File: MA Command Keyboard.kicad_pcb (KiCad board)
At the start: 2 copper layers, 195.3 x 209.6 mm, 165 parts, among them SW1 SW_Push, U1 ATmega32U4-A, Y1 16MHz

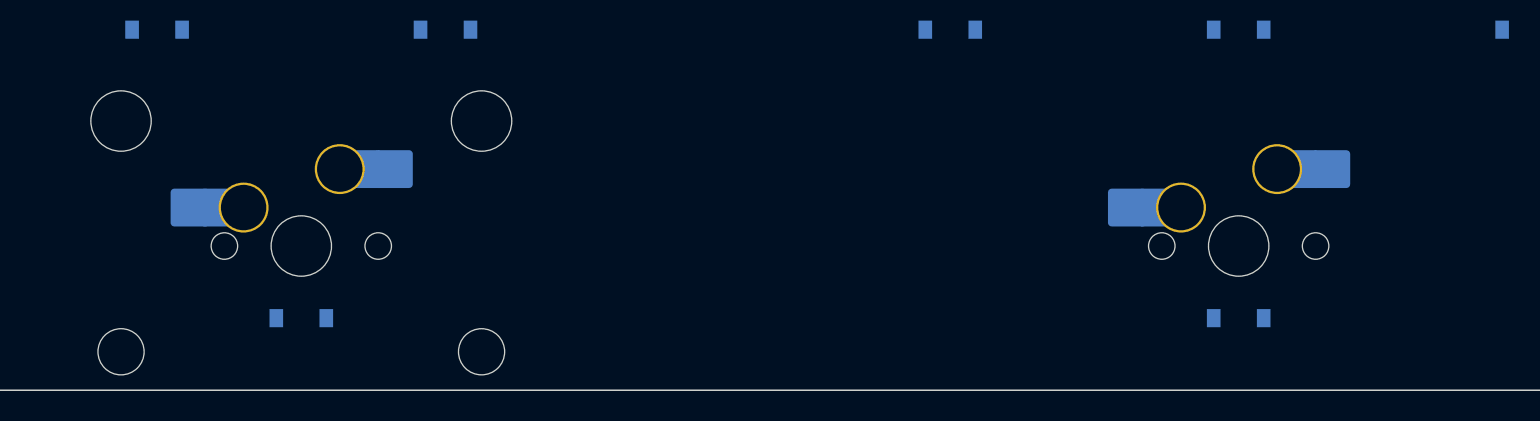
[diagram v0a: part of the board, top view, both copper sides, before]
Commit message: Updated Placement
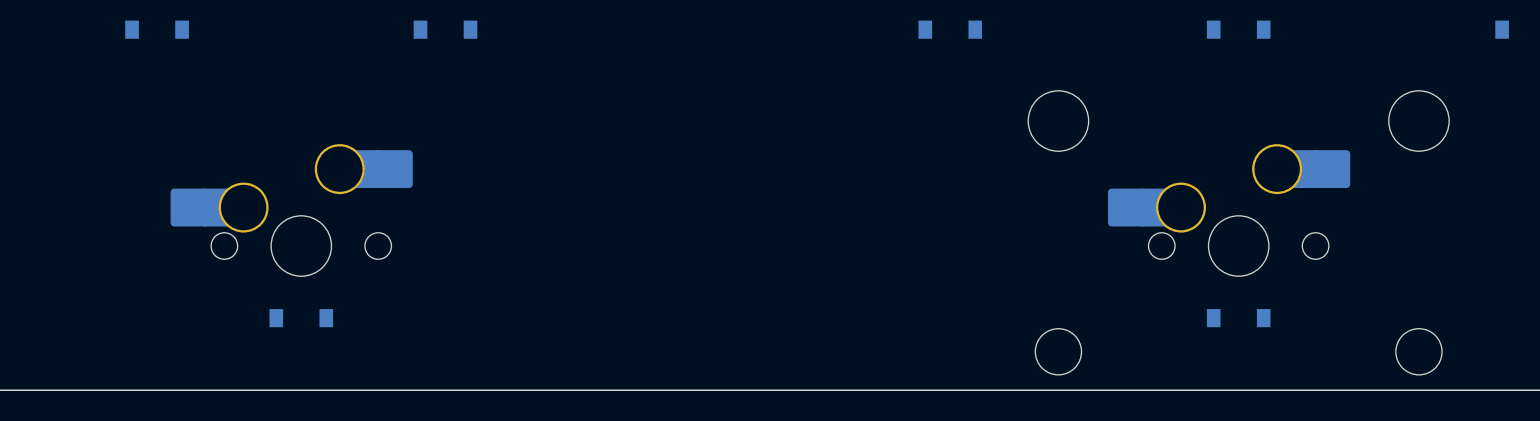
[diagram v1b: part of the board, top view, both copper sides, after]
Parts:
- moved D25 133.7 mm to (-327.0, 127.0)
- moved MX25 133.7 mm to (-327.0, 122.2)
- moved D63 114.7 mm to (-188.9, 231.8)
- moved MX63 114.7 mm to (-188.9, 227.0)
- moved D64 111.2 mm to (-169.9, 212.7)
- moved MX64 111.2 mm to (-169.9, 208.0)
- moved D65 109.5 mm to (-150.8, 231.8)
- moved MX65 109.5 mm to (-150.8, 227.0)
- moved D62 105.2 mm to (-222.2, 212.7)
- moved MX62 105.2 mm to (-222.2, 208.0)
- moved D71 95.2 mm to (-231.8, 250.8)
- moved MX71 95.2 mm to (-231.8, 246.1)
- moved D69 90.5 mm to (-260.4, 231.8)
- moved D70 90.5 mm to (-241.3, 231.8)
- moved MX69 90.5 mm to (-260.4, 227.0)
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
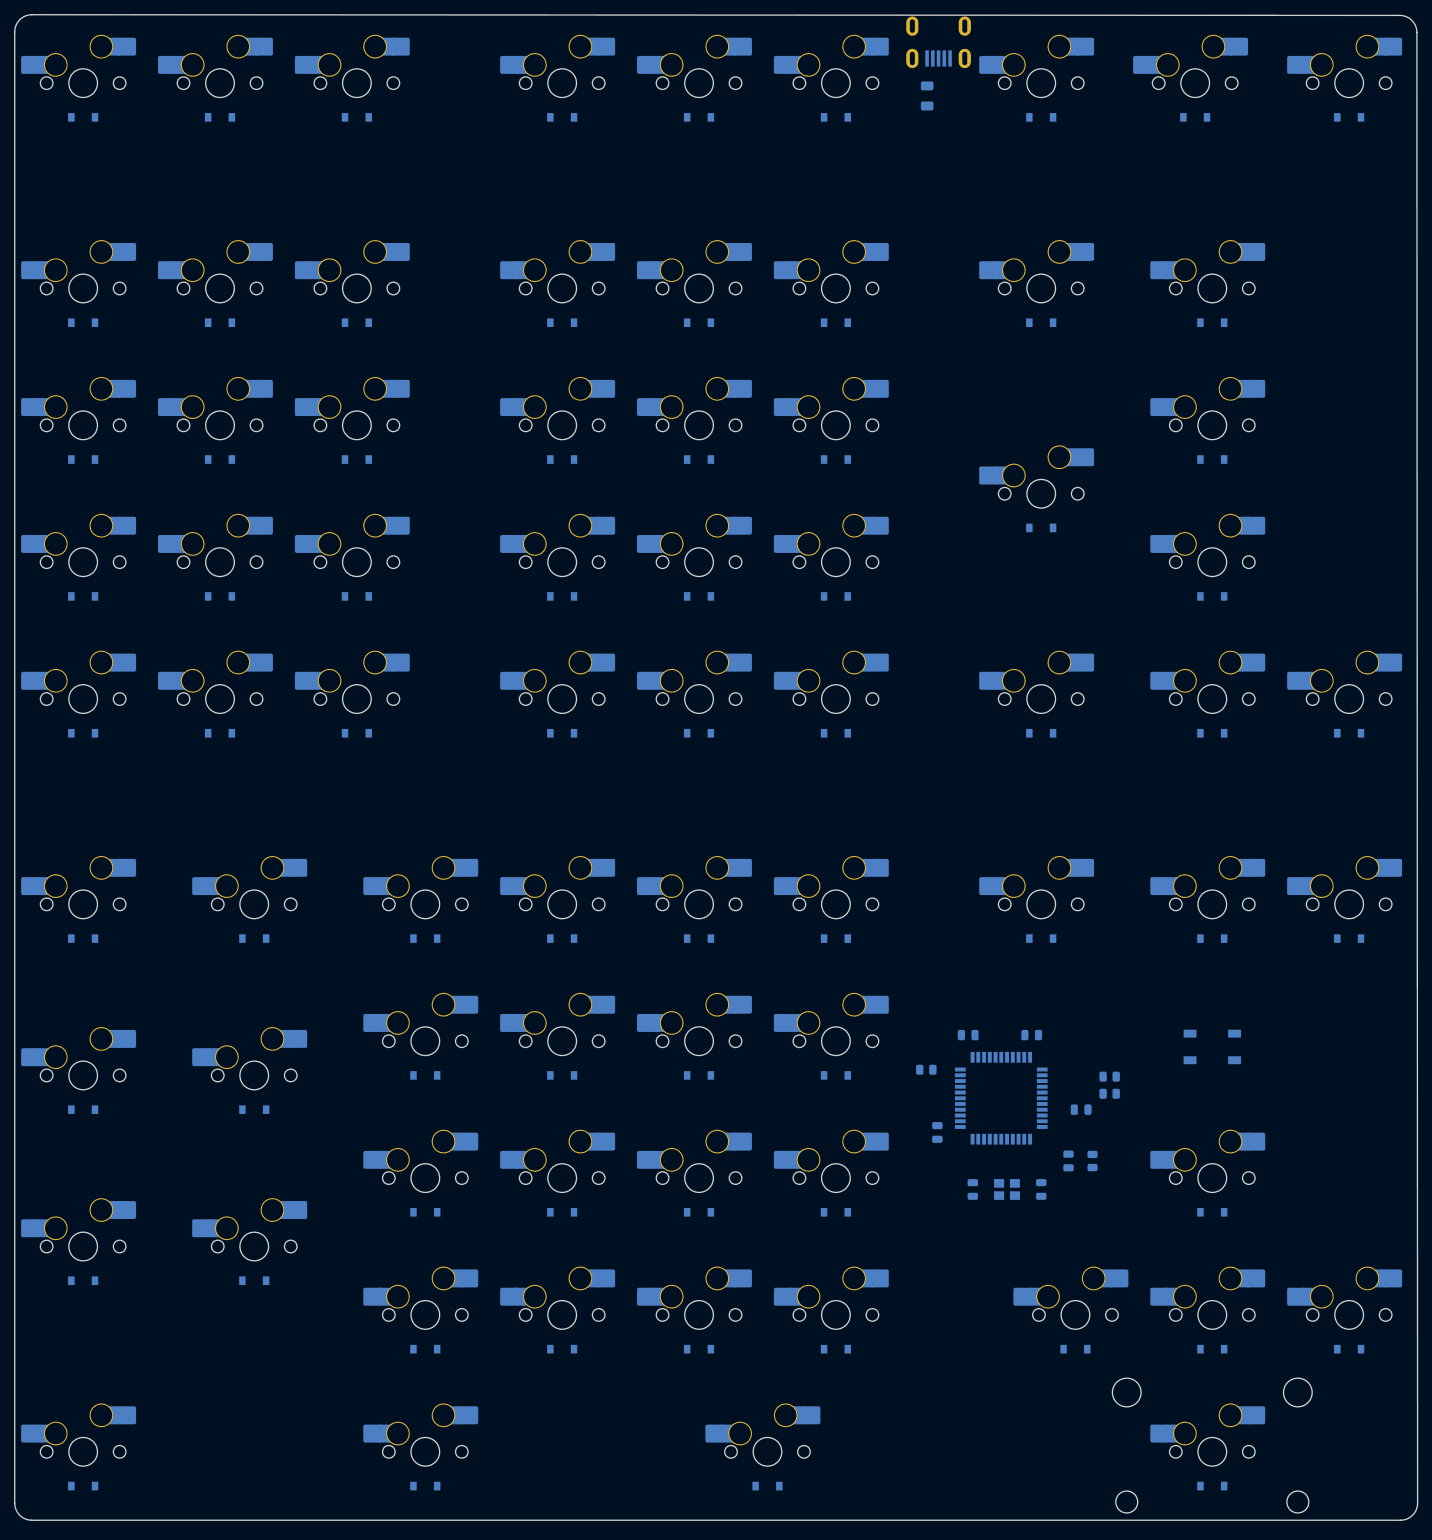
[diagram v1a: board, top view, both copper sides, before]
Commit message: Matrix Traces in
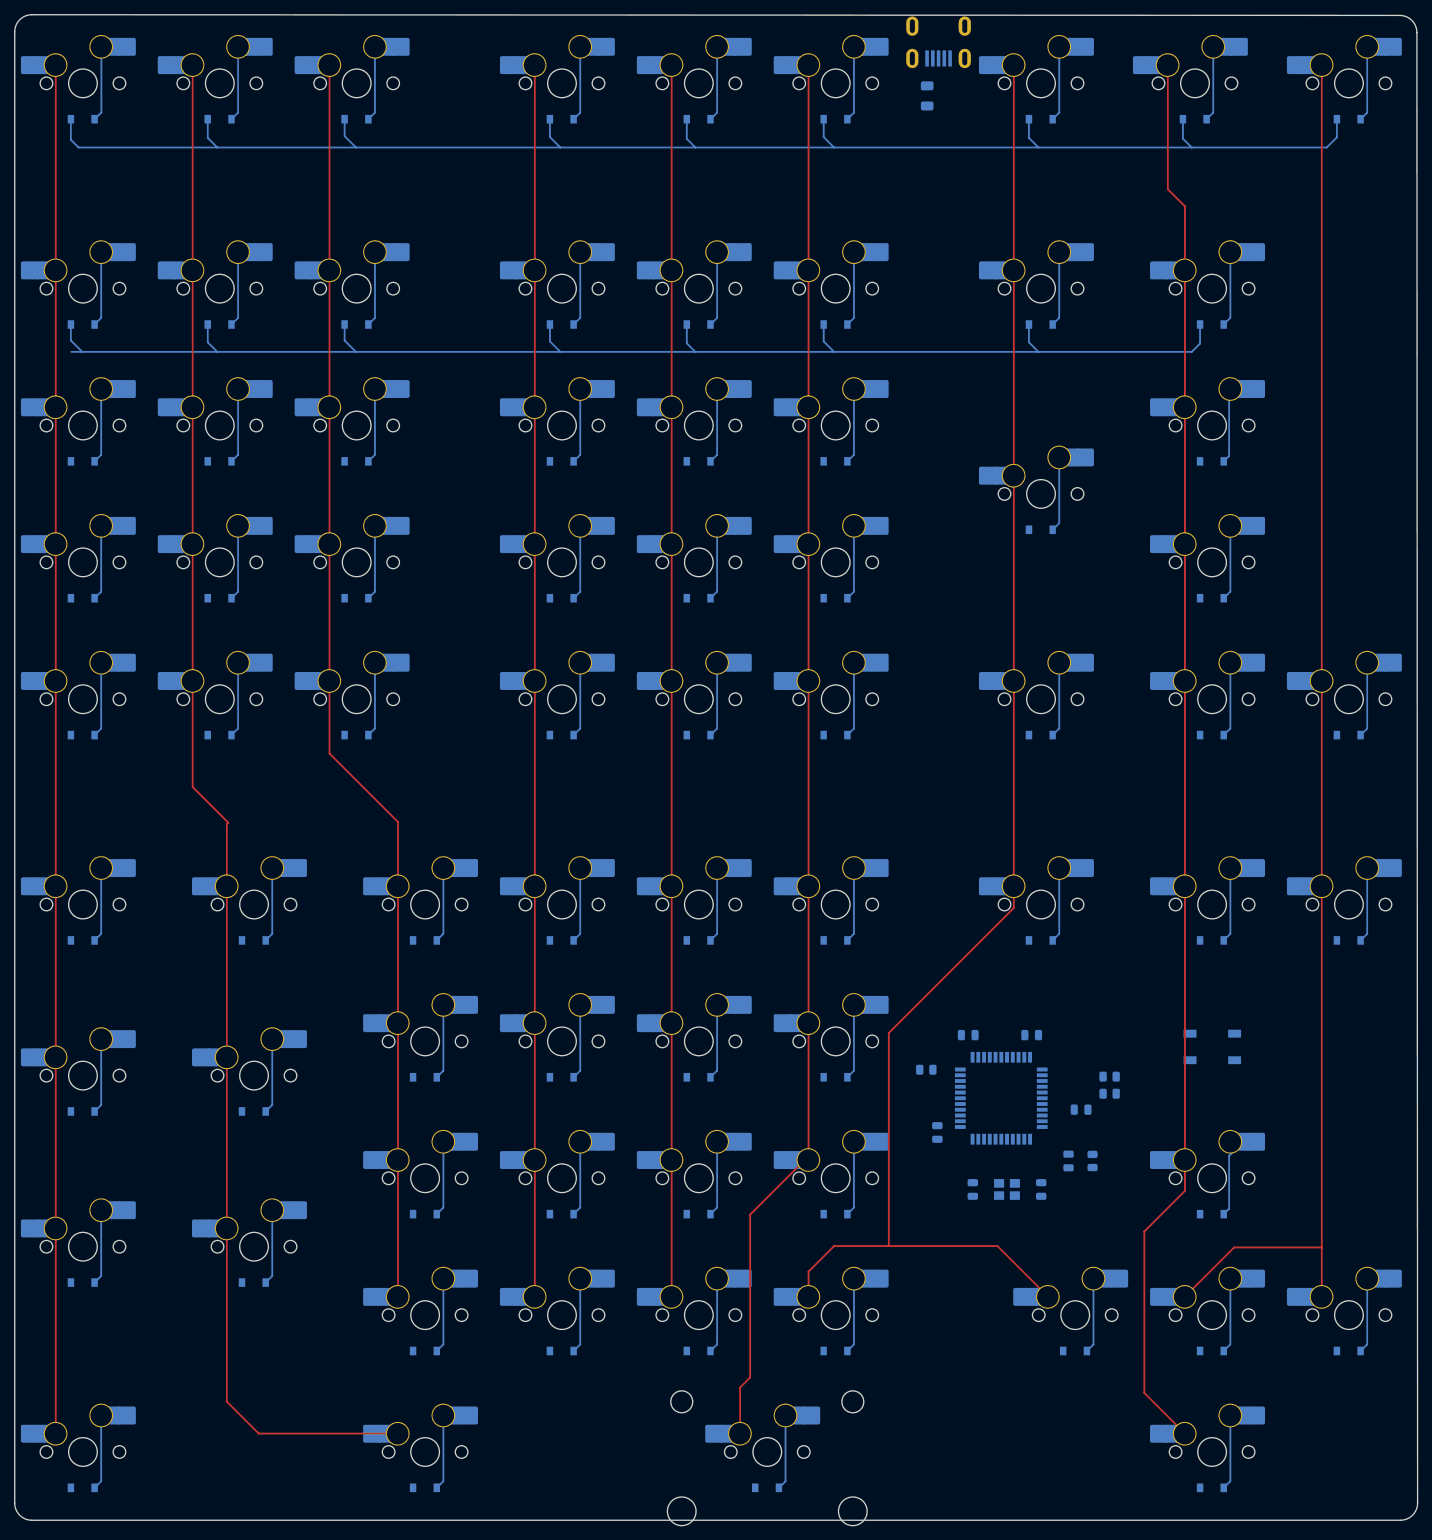
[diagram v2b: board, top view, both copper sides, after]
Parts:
- removed S73: MX_stab, marbastlib-mx:STAB_MX_2u
- added S71: MX_stab, marbastlib-mx:STAB_MX_2u, F.Cu at (-231.8, 246.1)
- moved D59 0.26 mm to (-279.5, 213.0), turned to 0 degrees
- moved D66 0.26 mm to (-327.1, 251.1), turned to 0 degrees
- moved D67 0.26 mm to (-279.5, 251.1), turned to 0 degrees
- moved D61 0.26 mm to (-241.4, 213.0), turned to 0 degrees
- moved D62 0.26 mm to (-222.3, 213.0), turned to 0 degrees
- moved D64 0.26 mm to (-169.9, 213.0), turned to 0 degrees
- moved D71 0.26 mm to (-231.8, 251.1), turned to 0 degrees
- moved D73 0.26 mm to (-169.9, 251.1), turned to 0 degrees
- moved D60 0.26 mm to (-260.4, 213.0), turned to 0 degrees
- moved D25 0.26 mm to (-327.1, 127.3), turned to 0 degrees
- moved D29 0.26 mm to (-241.4, 127.3), turned to 0 degrees
- moved D30 0.26 mm to (-222.3, 127.3), turned to 0 degrees
- moved D31 0.26 mm to (-193.7, 117.7), turned to 0 degrees
- moved D32 0.26 mm to (-169.9, 127.3), turned to 0 degrees
- moved D1 0.26 mm to (-327.1, 60.6), turned to 0 degrees
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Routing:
- net ROW0: track 0.00 -> 214.1 mm
- net cOL1: track 0.00 -> 213.8 mm
- net COL6: track 0.00 -> 212.8 mm
- net COL7: track 0.00 -> 196.2 mm
- net COL5: track 0.00 -> 194.7 mm
- net COL8: track 0.00 -> 193.3 mm
- net ROW1: track 0.00 -> 191.0 mm
- net COL0: track 0.00 -> 190.5 mm
- net COL2: track 0.00 -> 175.4 mm
- net COL4: track 0.00 -> 171.4 mm
- net COL3: track 0.00 -> 171.4 mm
- net Net-(D64-Pad2): track 0.00 -> 11.2 mm
- net Net-(D45-Pad2): track 0.00 -> 10.5 mm
- net Net-(D13-Pad2): track 0.00 -> 10.5 mm
- net Net-(D12-Pad2): track 0.00 -> 10.5 mm
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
